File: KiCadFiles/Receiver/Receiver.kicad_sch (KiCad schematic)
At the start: 9 parts, among them M1 Motor_DC, M2 Motor_DC, U1 MDD3A, U2 NRF24L01_Breakout, U3 ESP32-CAM

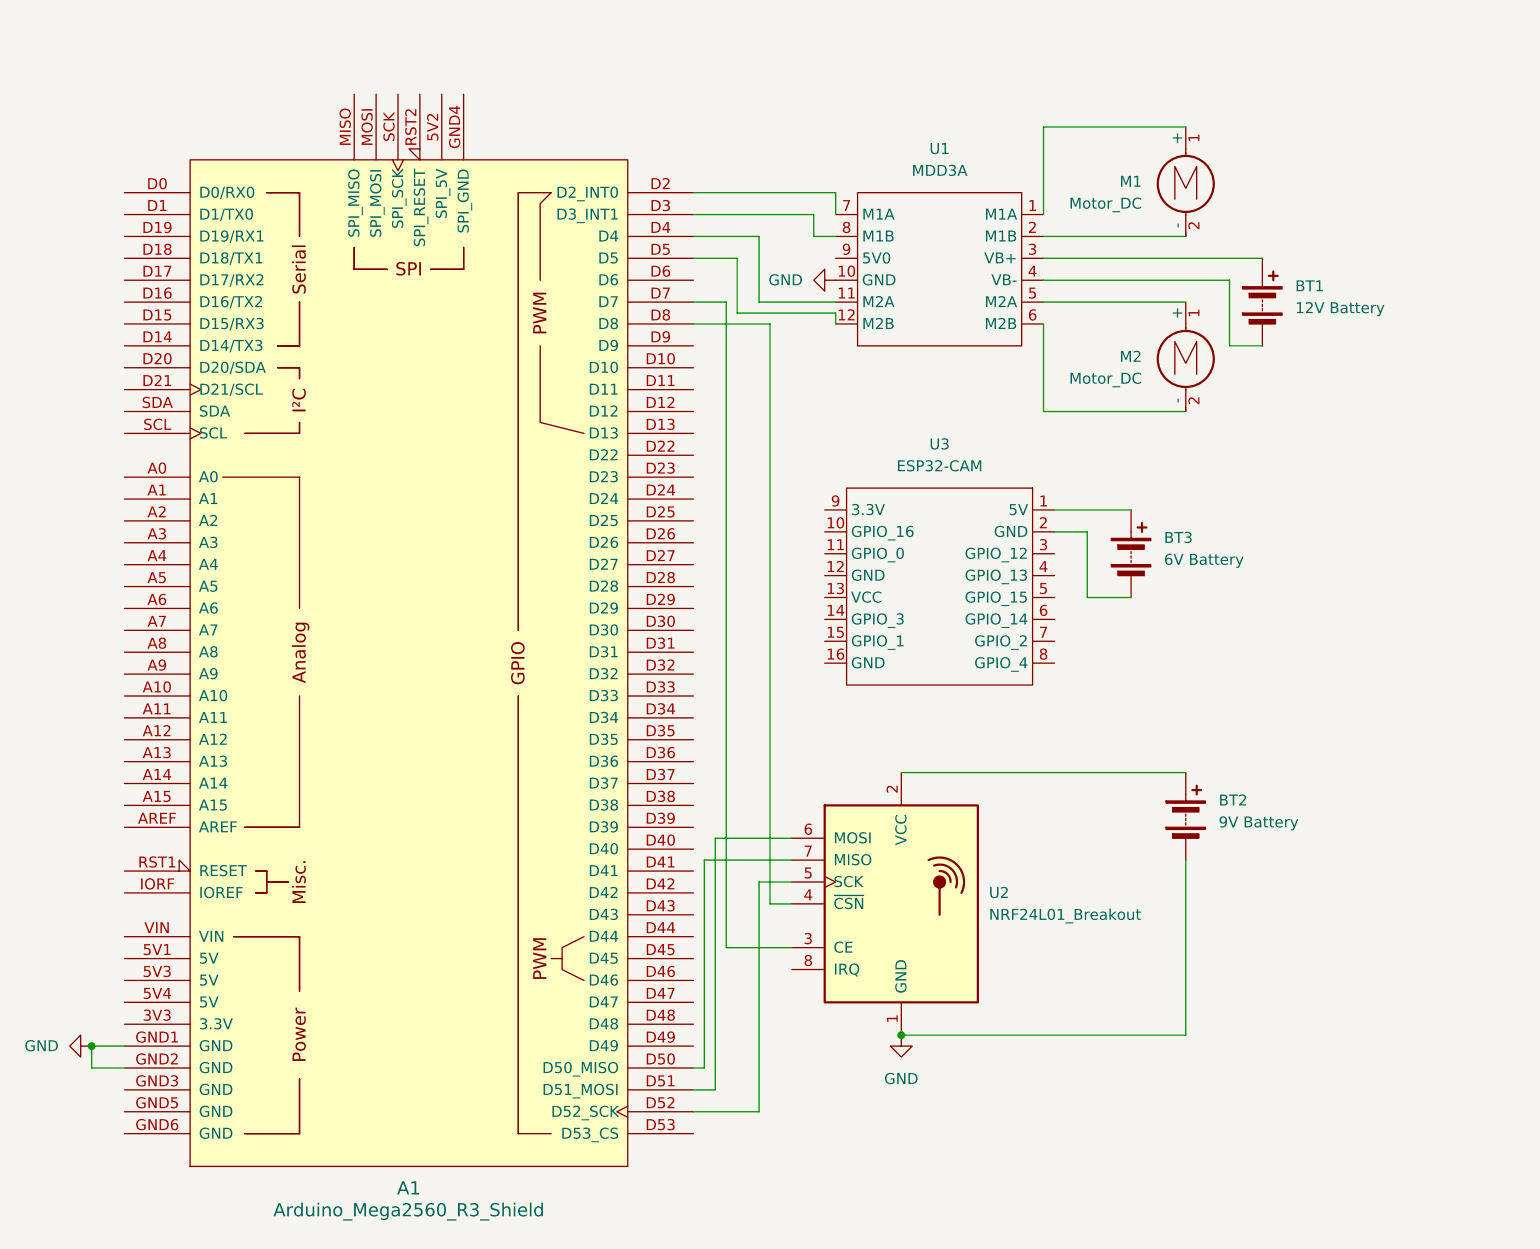
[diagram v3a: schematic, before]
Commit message: Update receiver schematic and fine-tuned receiver code
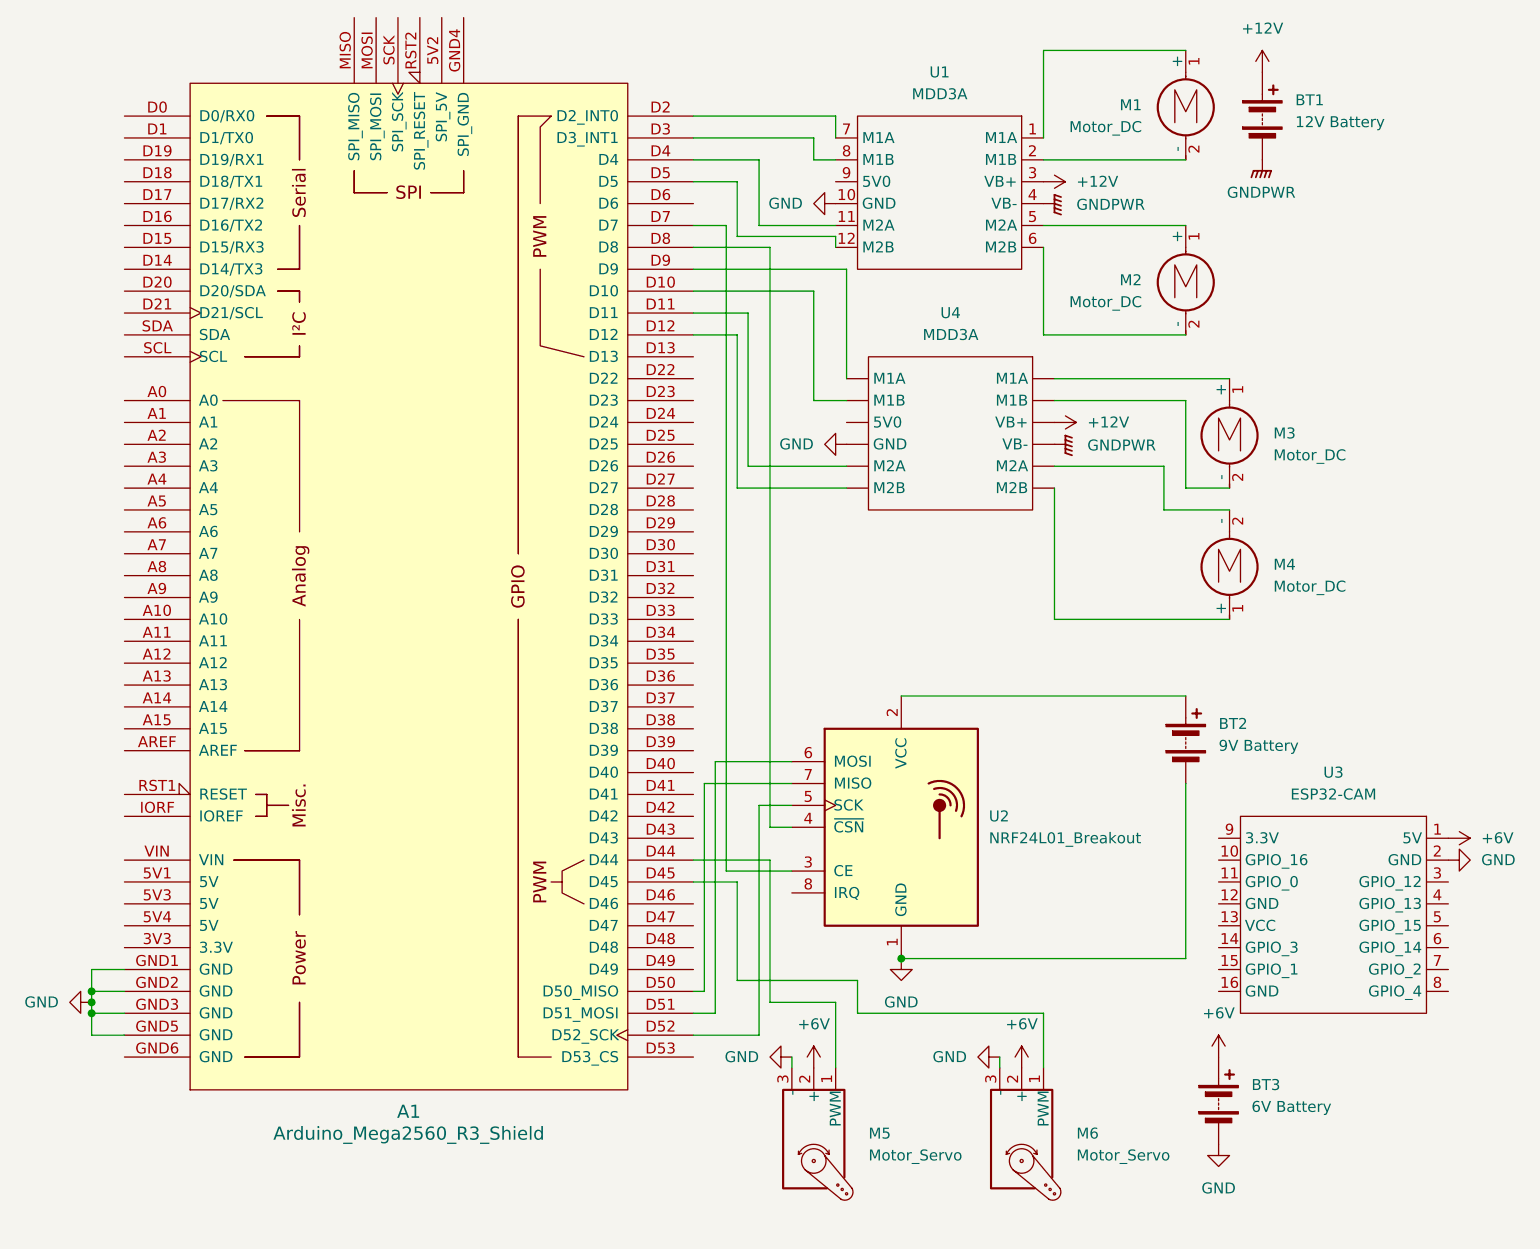
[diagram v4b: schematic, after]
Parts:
- added M3, M4: Motor_DC, symbol Motor:Motor_DC
- added M5, M6: Motor_Servo, symbol Motor:Motor_Servo
- added U4: MDD3A, symbol Breakout_Board_Library:MDD3A
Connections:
- net GND: now also A1.GND3 (GND), A1.GND5 (GND), BT3.2 (-), U3.2 (GND), M5.3 (-), M6.3 (-), U4.10 (GND)
- net +6V: now reaches BT3.1 (+), U3.1 (5V)
- net +6V: now also M5.2 (+), M6.2 (+)
- net +12V: now reaches BT1.1 (+), U1.3 (VB+)
- net +12V: now also U4.3 (VB+)
- net GNDPWR: now reaches BT1.2 (-), U1.4 (VB-)
- net GNDPWR: now also U4.4 (VB-)
- net at A1.D10: now also U4.8 (M1B)
- net at A1.D11: now also U4.11 (M2A)
- net at A1.D12: now also U4.12 (M2B)
- net at A1.D44: now also M5.1 (PWM)
- net at A1.D45: now also M6.1 (PWM)
- net at A1.D9: now also U4.7 (M1A)
- new net: M3.1 (+), U4.1 (M1A)
- new net: M3.2 (-), U4.2 (M1B)
- new net: M4.2 (-), U4.5 (M2A)
- new net: M4.1 (+), U4.6 (M2B)
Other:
- moved on the sheet: A1, BT1, BT2, BT3, M1, M2, U1, U2, U3
